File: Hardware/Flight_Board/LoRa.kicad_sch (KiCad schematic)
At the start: 1 part

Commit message: clean up and finalize initial design
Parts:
- added R25: 10k, symbol Device:R
- renumbered U8 to U9
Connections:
- net +3.3V: now also R25.1
- net at U9.1 (ANT_SW): now also R25.2
- net LORA_RST: now reaches U9.2 (NRST)
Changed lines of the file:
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@@
 (kicad_sch (version 20230121) (generator eeschema)
   (paper "A4")
+  (wire (pts (xy 116.84 88.9) (xy 119.38 88.9))
+    (stroke (width 0) (type default))
+  )
   (wire (pts (xy 142.24 91.44) (xy 144.78 91.44))
     (stroke (width 0) (type default))
@@
     (stroke (width 0) (type default))
   )
+  (wire (pts (xy 116.84 83.82) (xy 116.84 86.36))
+    (stroke (width 0) (type default))
+  )
   (wire (pts (xy 116.84 91.44) (xy 119.38 91.44))
     (stroke (width 0) (type default))
   )
   (wire (pts (xy 142.24 88.9) (xy 144.78 88.9))
+    (stroke (width 0) (type default))
+  )
+  (wire (pts (xy 116.84 86.36) (xy 119.38 86.36))
     (stroke (width 0) (type default))
   )
@@
     (effects (font (size 1.27 1.27)) (justify left))
   )
+  (hierarchical_label "LORA_RST" (shape input) (at 116.84 88.9 180) (fields_autoplaced)
+    (effects (font (size 1.27 1.27)) (justify right))
+  )
   (symbol (lib_id "Project:LR62E") (at 130.81 88.9 0) (unit 1)
     (in_bom yes) (on_board yes) (dnp no) (fields_autoplaced)
-    (property "Reference" "U8" (at 133.0041 81.28 0)
+    (property "Reference" "U9" (at 133.0041 81.28 0)
       (effects (font (size 1.27 1.27)) (justify left))
     )
@@
       (project "Flight_Board"
         (path "/e8eb85d5-f1ff-4500-895d-25b9ff5f6d36/7c06db2a-34f5-45c0-9668-fbbbd940678c"
-          (reference "U8") (unit 1)
+          (reference "U9") (unit 1)
+        )
+      )
+    )
+  )
+  (symbol (lib_id "Device:R") (at 116.84 80.01 0) (unit 1)
+    (in_bom yes) (on_board yes) (dnp no) (fields_autoplaced)
+    (property "Reference" "R25" (at 119.38 78.74 0)
+      (effects (font (size 1.27 1.27)) (justify left))
+    )
+    (property "Value" "10k" (at 119.38 81.28 0)
+      (effects (font (size 1.27 1.27)) (justify left))
+    )
+    (property "Footprint" "" (at 115.062 80.01 90)
+      (effects (font (size 1.27 1.27)) hide)
+    )
+    (property "Datasheet" "~" (at 116.84 80.01 0)
+      (effects (font (size 1.27 1.27)) hide)
+    )
+    (pin "1")
+    (pin "2")
+    (instances
+      (project "Flight_Board"
+        (path "/e8eb85d5-f1ff-4500-895d-25b9ff5f6d36/7c06db2a-34f5-45c0-9668-fbbbd940678c"
+          (reference "R25") (unit 1)
         )
       )
@@
   (symbol (lib_id "power:+3.3V") (at 130.81 77.47 0) (unit 1)
     (in_bom yes) (on_board yes) (dnp no) (fields_autoplaced)
-    (property "Reference" "#PWR040" (at 130.81 81.28 0)
+    (property "Reference" "#PWR057" (at 130.81 81.28 0)
       (effects (font (size 1.27 1.27)) hide)
     )
@@
       (project "Flight_Board"
         (path "/e8eb85d5-f1ff-4500-895d-25b9ff5f6d36/7c06db2a-34f5-45c0-9668-fbbbd940678c"
-          (reference "#PWR040") (unit 1)
+          (reference "#PWR057") (unit 1)
+        )
+      )
+    )
+  )
+  (symbol (lib_id "power:+3.3V") (at 116.84 76.2 0) (unit 1)
+    (in_bom yes) (on_board yes) (dnp no) (fields_autoplaced)
+    (property "Reference" "#PWR061" (at 116.84 80.01 0)
+      (effects (font (size 1.27 1.27)) hide)
+    )
+    (property "Value" "+3.3V" (at 116.84 71.12 0)
+      (effects (font (size 1.27 1.27)))
+    )
+    (property "Footprint" "" (at 116.84 76.2 0)
+      (effects (font (size 1.27 1.27)) hide)
+    )
+    (property "Datasheet" "" (at 116.84 76.2 0)
+      (effects (font (size 1.27 1.27)) hide)
+    )
+    (pin "1")
+    (instances
+      (project "Flight_Board"
+        (path "/e8eb85d5-f1ff-4500-895d-25b9ff5f6d36/7c06db2a-34f5-45c0-9668-fbbbd940678c"
+          (reference "#PWR061") (unit 1)
         )
       )
@@
   (symbol (lib_id "power:GND") (at 130.81 99.06 0) (unit 1)
     (in_bom yes) (on_board yes) (dnp no) (fields_autoplaced)
-    (property "Reference" "#PWR039" (at 130.81 105.41 0)
+    (property "Reference" "#PWR058" (at 130.81 105.41 0)
       (effects (font (size 1.27 1.27)) hide)
     )
@@
       (project "Flight_Board"
         (path "/e8eb85d5-f1ff-4500-895d-25b9ff5f6d36/7c06db2a-34f5-45c0-9668-fbbbd940678c"
-          (reference "#PWR039") (unit 1)
+          (reference "#PWR058") (unit 1)
         )
       )

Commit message: clean up, implement suggestions from saunders
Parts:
- added R31: 22k, symbol Device:R
- U9: value ~ -> LR62E
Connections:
- net +3.3V: now also R31.1
- net LORA_SDO: now also R31.2
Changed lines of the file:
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@@
 (kicad_sch (version 20230121) (generator eeschema)
   (paper "A4")
+  (junction (at 162.56 91.44) (diameter 0) (color 0 0 0 0)
+  )
   (wire (pts (xy 116.84 88.9) (xy 119.38 88.9))
     (stroke (width 0) (type default))
   )
-  (wire (pts (xy 142.24 91.44) (xy 144.78 91.44))
+  (wire (pts (xy 142.24 91.44) (xy 162.56 91.44))
+    (stroke (width 0) (type default))
+  )
+  (wire (pts (xy 162.56 87.63) (xy 162.56 91.44))
     (stroke (width 0) (type default))
   )
@@
   )
   (wire (pts (xy 142.24 86.36) (xy 144.78 86.36))
+    (stroke (width 0) (type default))
+  )
+  (wire (pts (xy 162.56 91.44) (xy 167.64 91.44))
     (stroke (width 0) (type default))
   )
@@
     (effects (font (size 1.27 1.27)) (justify right))
   )
-  (hierarchical_label "LORA_SDO" (shape output) (at 144.78 91.44 0) (fields_autoplaced)
+  (hierarchical_label "LORA_SDO" (shape output) (at 167.64 91.44 0) (fields_autoplaced)
     (effects (font (size 1.27 1.27)) (justify left))
   )
@@
   )
   (symbol (lib_id "Project:LR62E") (at 130.81 88.9 0) (unit 1)
-    (in_bom yes) (on_board yes) (dnp no) (fields_autoplaced)
-    (property "Reference" "U9" (at 133.0041 81.28 0)
-      (effects (font (size 1.27 1.27)) (justify left))
-    )
-    (property "Value" "~" (at 130.81 88.9 0)
+    (in_bom yes) (on_board yes) (dnp no)
+    (property "Reference" "U9" (at 135.89 80.01 0)
+      (effects (font (size 1.27 1.27)) (justify left))
+    )
+    (property "Value" "LR62E" (at 137.16 82.55 0)
       (effects (font (size 1.27 1.27)))
     )
@@
         )
       )
+    )
+  )
+  (symbol (lib_id "power:+3.3V") (at 162.56 80.01 0) (unit 1)
+    (in_bom yes) (on_board yes) (dnp no) (fields_autoplaced)
+    (property "Reference" "#PWR068" (at 162.56 83.82 0)
+      (effects (font (size 1.27 1.27)) hide)
+    )
+    (property "Value" "+3.3V" (at 162.56 74.93 0)
+      (effects (font (size 1.27 1.27)))
+    )
+    (property "Footprint" "" (at 162.56 80.01 0)
+      (effects (font (size 1.27 1.27)) hide)
+    )
+    (property "Datasheet" "" (at 162.56 80.01 0)
+      (effects (font (size 1.27 1.27)) hide)
+    )
+    (pin "1")
+    (instances
+      (project "Flight_Board"
+        (path "/e8eb85d5-f1ff-4500-895d-25b9ff5f6d36"
+          (reference "#PWR068") (unit 1)
+        )
+        (path "/e8eb85d5-f1ff-4500-895d-25b9ff5f6d36/7c06db2a-34f5-45c0-9668-fbbbd940678c"
+          (reference "#PWR069") (unit 1)
+        )
+      )
+    )
+  )
+  (symbol (lib_id "Device:R") (at 162.56 83.82 0) (unit 1)
+    (in_bom yes) (on_board yes) (dnp no) (fields_autoplaced)
+    (property "Reference" "R31" (at 165.1 82.55 0)
+      (effects (font (size 1.27 1.27)) (justify left))
+    )
+    (property "Value" "22k" (at 165.1 85.09 0)
+      (effects (font (size 1.27 1.27)) (justify left))
+    )
+    (property "Footprint" "" (at 160.782 83.82 90)
+      (effects (font (size 1.27 1.27)) hide)
+    )
+    (property "Datasheet" "~" (at 162.56 83.82 0)
+      (effects (font (size 1.27 1.27)) hide)
+    )
+    (pin "1")
+    (pin "2")
+    (instances
+      (project "Flight_Board"
+        (path "/e8eb85d5-f1ff-4500-895d-25b9ff5f6d36"
+          (reference "R31") (unit 1)
+        )
+        (path "/e8eb85d5-f1ff-4500-895d-25b9ff5f6d36/7c06db2a-34f5-45c0-9668-fbbbd940678c"
+          (reference "R32") (unit 1)
+        )
+      )

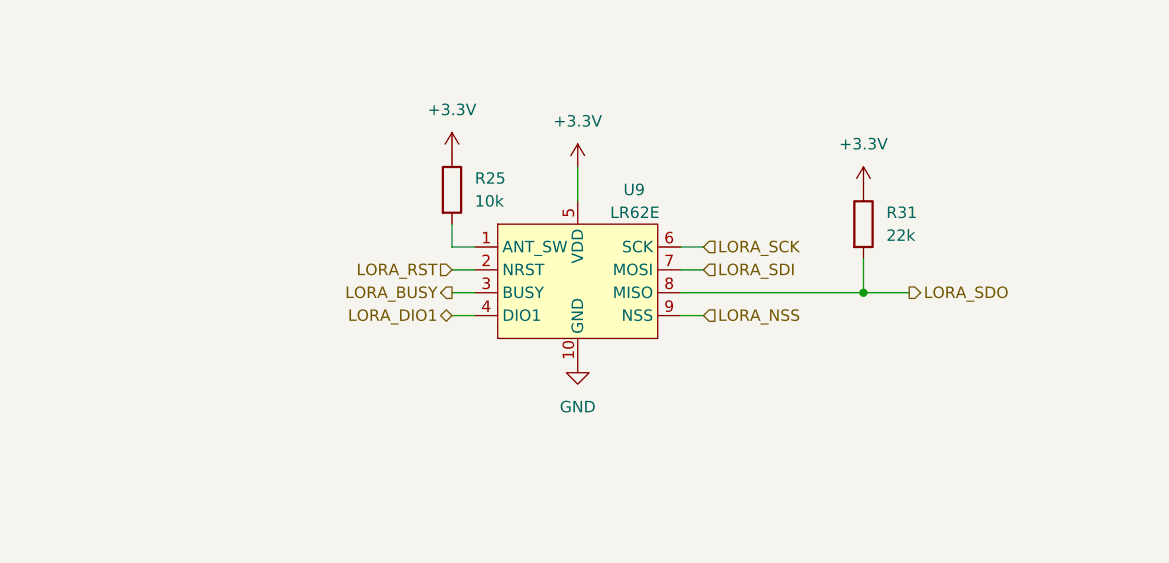
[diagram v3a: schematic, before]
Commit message: Add LEDs and test points
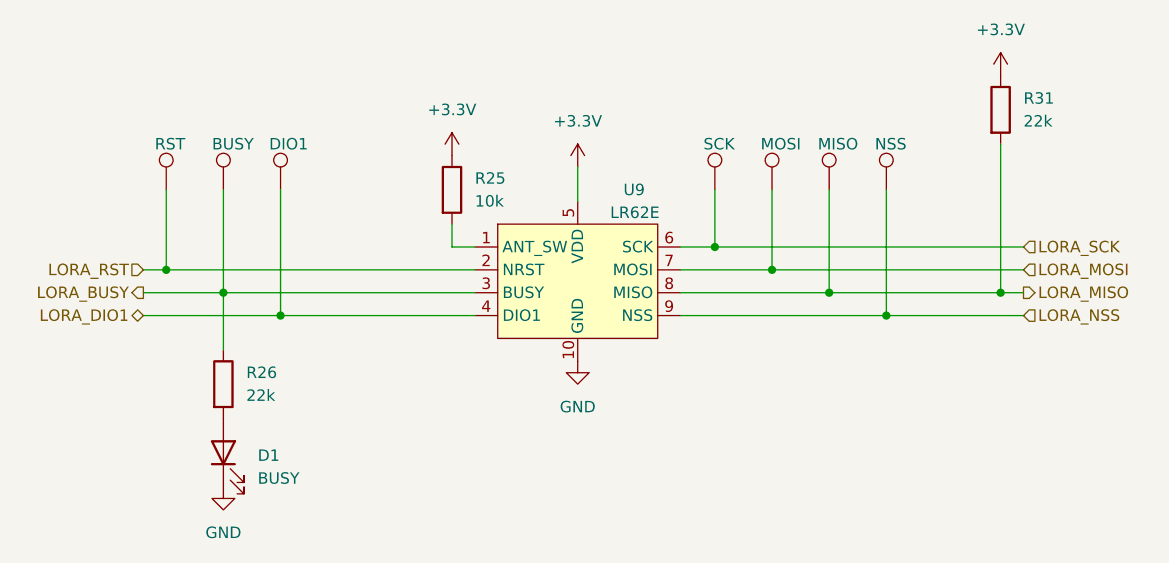
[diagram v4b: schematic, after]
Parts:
- added D1: BUSY, symbol Device:LED
- added R26: 22k, symbol Device:R
- added TP2: SCK, symbol Connector:TestPoint
- added TP2: BUSY, symbol Connector:TestPoint
- added TP2: NSS, symbol Connector:TestPoint
- added TP2: MISO, symbol Connector:TestPoint
- added TP2: DIO1, symbol Connector:TestPoint
- added TP2: RST, symbol Connector:TestPoint
- added TP2: MOSI, symbol Connector:TestPoint
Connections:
- net GND: now also D1.1 (K)
- net LORA_BUSY: now also R26.1, TP2.1
- net LORA_DIO1: now also TP2.1
- net LORA_NSS: now also TP2.1
- net LORA_RST: now also TP2.1
- net LORA_SCK: now also TP2.1
- net LORA_SDI renamed LORA_MOSI
- net LORA_MOSI: now also TP2.1
- net LORA_SDO renamed LORA_MISO
- net LORA_MISO: now also TP2.1
- new net: D1.2 (A), R26.2
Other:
- moved on the sheet: R31

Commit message: final touches, bom, footprints
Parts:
- D1: footprint (none) -> LED_SMD:LED_0603_1608Metric_Pad1.05x0.95mm_HandSolder
- R25, R26, R31: footprint (none) -> Resistor_SMD:R_0603_1608Metric_Pad0.98x0.95mm_HandSolder
- TP2: footprint (none) -> TestPoint:TestPoint_THTPad_2.0x2.0mm_Drill1.0mm
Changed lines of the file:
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@@
       (effects (font (size 1.27 1.27)) (justify left))
     )
-    (property "Footprint" "" (at 151.13 80.01 0)
+    (property "Footprint" "TestPoint:TestPoint_THTPad_2.0x2.0mm_Drill1.0mm" (at 151.13 80.01 0)
       (effects (font (size 1.27 1.27)) hide)
     )
@@
       (effects (font (size 1.27 1.27)) (justify left))
     )
-    (property "Footprint" "" (at 96.52 80.01 0)
+    (property "Footprint" "TestPoint:TestPoint_THTPad_2.0x2.0mm_Drill1.0mm" (at 96.52 80.01 0)
       (effects (font (size 1.27 1.27)) hide)
     )
@@
       (effects (font (size 1.27 1.27)) (justify left))
     )
-    (property "Footprint" "" (at 115.062 80.01 90)
+    (property "Footprint" "Resistor_SMD:R_0603_1608Metric_Pad0.98x0.95mm_HandSolder" (at 115.062 80.01 90)
       (effects (font (size 1.27 1.27)) hide)
     )
@@
       (effects (font (size 1.27 1.27)) (justify left))
     )
-    (property "Footprint" "" (at 170.18 80.01 0)
+    (property "Footprint" "TestPoint:TestPoint_THTPad_2.0x2.0mm_Drill1.0mm" (at 170.18 80.01 0)
       (effects (font (size 1.27 1.27)) hide)
     )
@@
       (effects (font (size 1.27 1.27)) (justify left))
     )
-    (property "Footprint" "" (at 163.83 80.01 0)
+    (property "Footprint" "TestPoint:TestPoint_THTPad_2.0x2.0mm_Drill1.0mm" (at 163.83 80.01 0)
       (effects (font (size 1.27 1.27)) hide)
     )
@@
       (effects (font (size 1.27 1.27)) (justify right))
     )
-    (property "Footprint" "" (at 91.44 109.22 0)
+    (property "Footprint" "LED_SMD:LED_0603_1608Metric_Pad1.05x0.95mm_HandSolder" (at 91.44 109.22 0)
       (effects (font (size 1.27 1.27)) hide)
     )
@@
       (effects (font (size 1.27 1.27)) (justify left))
     )
-    (property "Footprint" "" (at 102.87 80.01 0)
+    (property "Footprint" "TestPoint:TestPoint_THTPad_2.0x2.0mm_Drill1.0mm" (at 102.87 80.01 0)
       (effects (font (size 1.27 1.27)) hide)
     )
@@
       (effects (font (size 1.27 1.27)) (justify left))
     )
-    (property "Footprint" "" (at 90.17 80.01 0)
+    (property "Footprint" "TestPoint:TestPoint_THTPad_2.0x2.0mm_Drill1.0mm" (at 90.17 80.01 0)
       (effects (font (size 1.27 1.27)) hide)
     )
@@
       (effects (font (size 1.27 1.27)) (justify left))
     )
-    (property "Footprint" "" (at 89.662 101.6 90)
+    (property "Footprint" "Resistor_SMD:R_0603_1608Metric_Pad0.98x0.95mm_HandSolder" (at 89.662 101.6 90)
       (effects (font (size 1.27 1.27)) hide)
     )
@@
       (effects (font (size 1.27 1.27)) (justify left))
     )
-    (property "Footprint" "" (at 176.022 71.12 90)
+    (property "Footprint" "Resistor_SMD:R_0603_1608Metric_Pad0.98x0.95mm_HandSolder" (at 176.022 71.12 90)
       (effects (font (size 1.27 1.27)) hide)
     )
@@
       (effects (font (size 1.27 1.27)) (justify left))
     )
-    (property "Footprint" "" (at 157.48 80.01 0)
-      (effects (font (size 1.27 1.27)) hide)
-    )
+    (property "Footprint" "TestPoint:TestPoint_THTPad_2.0x2.0mm_Drill1.0mm" (at 157.48 80.01 0)
+      (effects (font (size 1.27 1.27)) hide)
+    )

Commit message: initial placement on board, continue routing
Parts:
- removed TP2: SCK, TestPoint:TestPoint_THTPad_2.0x2.0mm_Drill1.0mm, symbol Connector:TestPoint
- removed TP2: BUSY, TestPoint:TestPoint_THTPad_2.0x2.0mm_Drill1.0mm, symbol Connector:TestPoint
- removed TP2: NSS, TestPoint:TestPoint_THTPad_2.0x2.0mm_Drill1.0mm, symbol Connector:TestPoint
- removed TP2: MISO, TestPoint:TestPoint_THTPad_2.0x2.0mm_Drill1.0mm, symbol Connector:TestPoint
- removed TP2: DIO1, TestPoint:TestPoint_THTPad_2.0x2.0mm_Drill1.0mm, symbol Connector:TestPoint
- removed TP2: RST, TestPoint:TestPoint_THTPad_2.0x2.0mm_Drill1.0mm, symbol Connector:TestPoint
- removed TP2: MOSI, TestPoint:TestPoint_THTPad_2.0x2.0mm_Drill1.0mm, symbol Connector:TestPoint

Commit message: initial route of 4-layer board
ouch
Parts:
- renumbered D1 to D3, R26 to R28, R25 to R29
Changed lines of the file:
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@@
   (symbol (lib_id "Device:R") (at 116.84 80.01 0) (unit 1)
     (in_bom yes) (on_board yes) (dnp no) (fields_autoplaced)
-    (property "Reference" "R25" (at 119.38 78.74 0)
+    (property "Reference" "R29" (at 119.38 78.74 0)
       (effects (font (size 1.27 1.27)) (justify left))
     )
@@
       (project "Flight_Board"
         (path "/e8eb85d5-f1ff-4500-895d-25b9ff5f6d36/7c06db2a-34f5-45c0-9668-fbbbd940678c"
-          (reference "R25") (unit 1)
+          (reference "R29") (unit 1)
         )
       )
@@
   (symbol (lib_id "power:+3.3V") (at 130.81 77.47 0) (unit 1)
     (in_bom yes) (on_board yes) (dnp no) (fields_autoplaced)
-    (property "Reference" "#PWR061" (at 130.81 81.28 0)
+    (property "Reference" "#PWR067" (at 130.81 81.28 0)
       (effects (font (size 1.27 1.27)) hide)
     )
@@
       (project "Flight_Board"
         (path "/e8eb85d5-f1ff-4500-895d-25b9ff5f6d36/7c06db2a-34f5-45c0-9668-fbbbd940678c"
-          (reference "#PWR061") (unit 1)
+          (reference "#PWR067") (unit 1)
         )
       )
@@
   (symbol (lib_id "power:+3.3V") (at 116.84 76.2 0) (unit 1)
     (in_bom yes) (on_board yes) (dnp no) (fields_autoplaced)
-    (property "Reference" "#PWR060" (at 116.84 80.01 0)
+    (property "Reference" "#PWR066" (at 116.84 80.01 0)
       (effects (font (size 1.27 1.27)) hide)
     )
@@
       (project "Flight_Board"
         (path "/e8eb85d5-f1ff-4500-895d-25b9ff5f6d36/7c06db2a-34f5-45c0-9668-fbbbd940678c"
-          (reference "#PWR060") (unit 1)
+          (reference "#PWR066") (unit 1)
         )
       )
@@
   (symbol (lib_id "power:GND") (at 130.81 99.06 0) (unit 1)
     (in_bom yes) (on_board yes) (dnp no) (fields_autoplaced)
-    (property "Reference" "#PWR062" (at 130.81 105.41 0)
+    (property "Reference" "#PWR068" (at 130.81 105.41 0)
       (effects (font (size 1.27 1.27)) hide)
     )
@@
       (project "Flight_Board"
         (path "/e8eb85d5-f1ff-4500-895d-25b9ff5f6d36/7c06db2a-34f5-45c0-9668-fbbbd940678c"
-          (reference "#PWR062") (unit 1)
+          (reference "#PWR068") (unit 1)
         )
       )
@@
   (symbol (lib_id "Device:LED") (at 91.44 109.22 90) (unit 1)
     (in_bom yes) (on_board yes) (dnp no) (fields_autoplaced)
-    (property "Reference" "D1" (at 95.25 109.5375 90)
+    (property "Reference" "D3" (at 95.25 109.5375 90)
       (effects (font (size 1.27 1.27)) (justify right))
     )
@@
       (project "Flight_Board"
         (path "/e8eb85d5-f1ff-4500-895d-25b9ff5f6d36/7c06db2a-34f5-45c0-9668-fbbbd940678c"
-          (reference "D1") (unit 1)
+          (reference "D3") (unit 1)
         )
       )
@@
   (symbol (lib_id "Device:R") (at 91.44 101.6 0) (unit 1)
     (in_bom yes) (on_board yes) (dnp no) (fields_autoplaced)
-    (property "Reference" "R26" (at 93.98 100.33 0)
+    (property "Reference" "R28" (at 93.98 100.33 0)
       (effects (font (size 1.27 1.27)) (justify left))
     )
@@
       (project "Flight_Board"
         (path "/e8eb85d5-f1ff-4500-895d-25b9ff5f6d36/7c06db2a-34f5-45c0-9668-fbbbd940678c"
-          (reference "R26") (unit 1)
+          (reference "R28") (unit 1)
         )
       )
@@
   (symbol (lib_id "power:GND") (at 91.44 113.03 0) (unit 1)
     (in_bom yes) (on_board yes) (dnp no) (fields_autoplaced)
-    (property "Reference" "#PWR063" (at 91.44 119.38 0)
+    (property "Reference" "#PWR065" (at 91.44 119.38 0)
       (effects (font (size 1.27 1.27)) hide)
     )
@@
       (project "Flight_Board"
         (path "/e8eb85d5-f1ff-4500-895d-25b9ff5f6d36/7c06db2a-34f5-45c0-9668-fbbbd940678c"
-          (reference "#PWR063") (unit 1)
+          (reference "#PWR065") (unit 1)
         )
       )
@@
         )
         (path "/e8eb85d5-f1ff-4500-895d-25b9ff5f6d36/7c06db2a-34f5-45c0-9668-fbbbd940678c"
-          (reference "R32") (unit 1)
-        )
-      )
+          (reference "R30") (unit 1)
+        )
+      )
